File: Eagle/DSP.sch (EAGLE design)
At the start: 4 parts

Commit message: added lots of parts and connected things
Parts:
- added C4, C5: 0.1uF, kiss_z:C0603
- added D1: KWL-R1025VB, kiss_z:KWL-R1025VB
- added J1, J2, J4, J5: (no value), SparkFun-Connectors:CONN_02
- added J3: (no value), SparkFun-Connectors:CONN_11
- added R1: 4611X-101-102LF, kiss_z:4611X-101-102LF
- added R2, R3: 100K, kiss_z:R0603
- added U$1: NHD-C12864A1Z-FSW-FBW-HTT, kiss_z:NHD-C12864A1Z-FSW-FBW-HTT
- C2: value 0.1uF -> 0.22uF
- C3: value (none) -> 0.1uF
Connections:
- new net 18: J3.6, TEENSY_3.2.18
- new net 19: J3.7, TEENSY_3.2.19
- new net 20: J3.8, TEENSY_3.2.20
- new net 21: J3.9, TEENSY_3.2.21
- new net 22: J3.10, TEENSY_3.2.22
- new net ADC_IN: C2.2, J3.11, R2.2, R3.1, TEENSY_3.2.23
- new net CS_LCD: TEENSY_3.2.10, U$1./CS
- new net CS_PLL: J3.5, TEENSY_3.2.17
- new net CS_POT: J3.4, TEENSY_3.2.16
- new net DAC_OUT: C3.2, J2.1
- new net MISO: TEENSY_3.2.12
- new net MOSI: TEENSY_3.2.11, U$1.MOSI
- new net N$10: D1.P$8, R1.9
- new net N$11: D1.P$9, R1.10
- new net N$12: D1.P$10, R1.11
- new net N$13: D1.P$20, TEENSY_3.2.0
- new net N$14: D1.P$19, TEENSY_3.2.1
- new net N$15: D1.P$18, TEENSY_3.2.2
- new net N$16: D1.P$17, TEENSY_3.2.3
- new net N$17: D1.P$16, TEENSY_3.2.4
- new net N$18: D1.P$15, TEENSY_3.2.5
- new net N$19: D1.P$14, TEENSY_3.2.6
- new net N$20: D1.P$13, TEENSY_3.2.7
- new net N$21: D1.P$12, TEENSY_3.2.8
- new net N$22: D1.P$11, TEENSY_3.2.9
- new net N$3: D1.P$1, R1.2
- new net N$4: D1.P$2, R1.3
- new net N$5: D1.P$3, R1.4
- new net N$6: D1.P$4, R1.5
- new net N$7: D1.P$5, R1.6
- new net N$8: D1.P$6, R1.7
- new net N$9: D1.P$7, R1.8
- new net RDR_IN: C2.1, J5.1
- new net REG_LCD: TEENSY_3.2.15, U$1.A0
- new net RST_LCD: TEENSY_3.2.14, U$1./RESET
- new net SCLK: J3.3, TEENSY_3.2.13, U$1.SCLK
- net +3V3: now also C1.1, C5.1, J3.1, J4.1, R1.1, R2.1, U$1.LED+, U$1.VDD; no longer C2.1
- net +5V: now also C4.1, J1.1; no longer C1.1
- net GND: now also C4.2, C5.2, J1.2, J2.2, J3.2, J4.2, J5.2, R3.2, U$1.H-, U$1.LED-, U$1.VSS; no longer C2.2
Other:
- moved on the sheet: C1, C2, C3

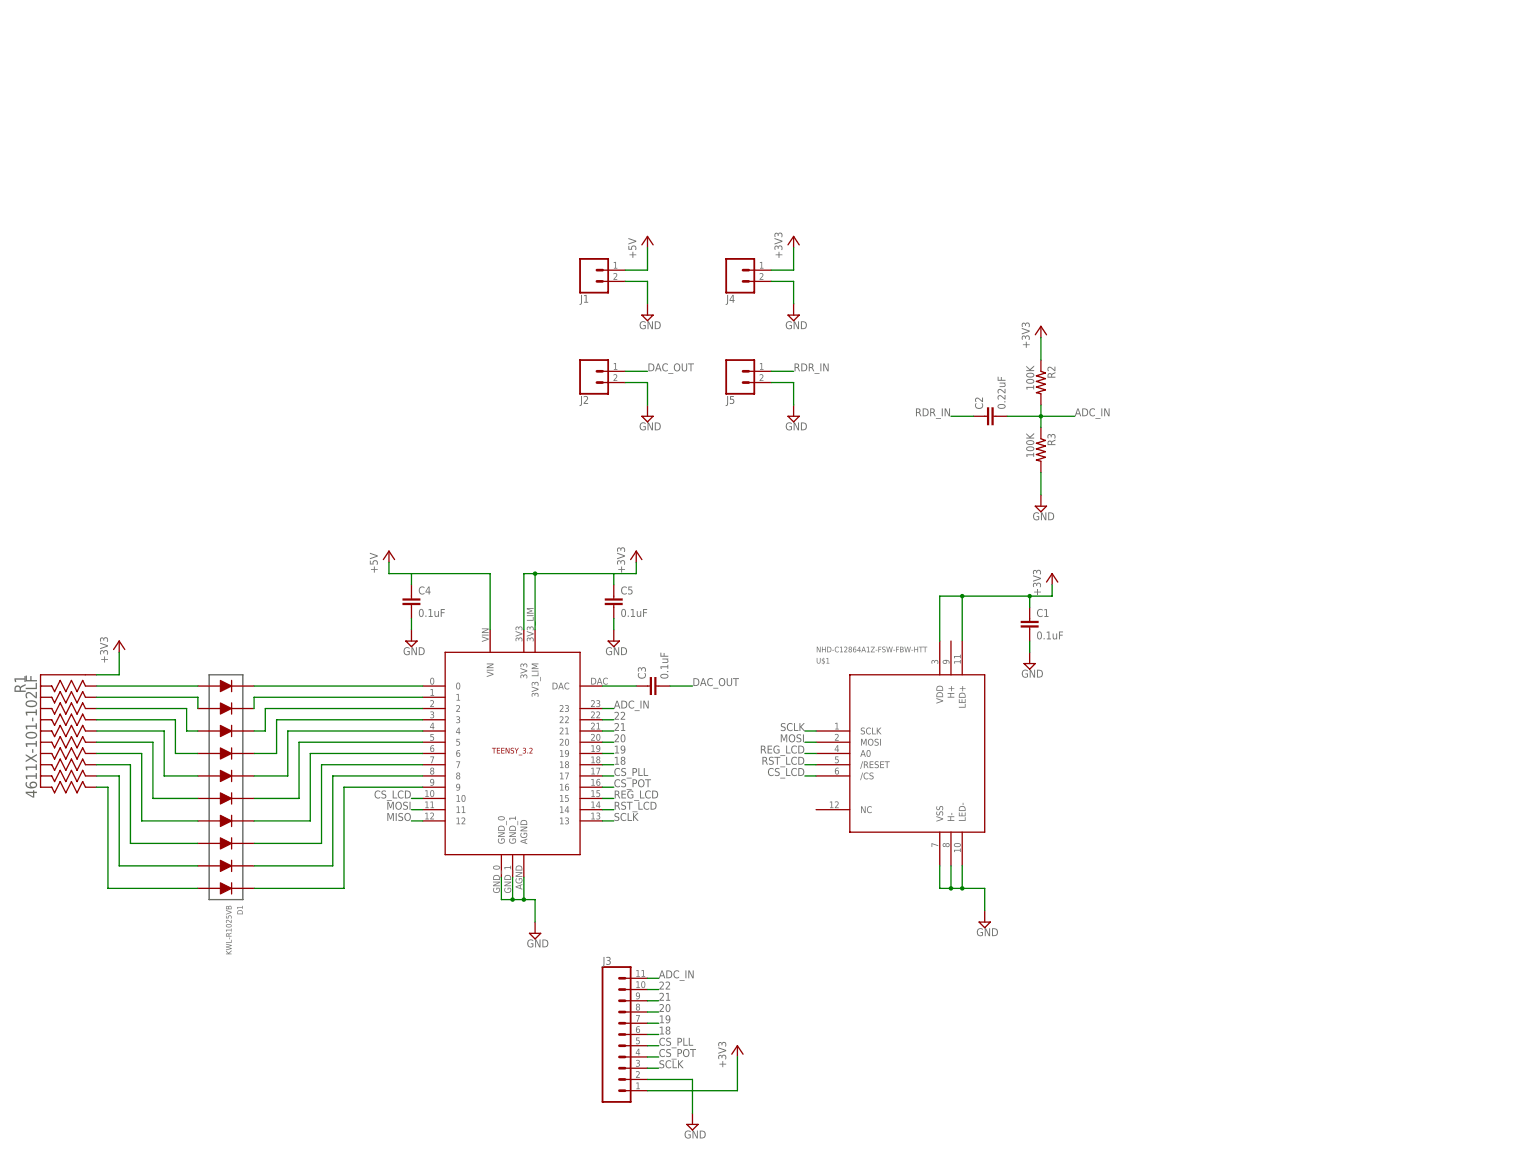
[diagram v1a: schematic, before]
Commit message: added switches
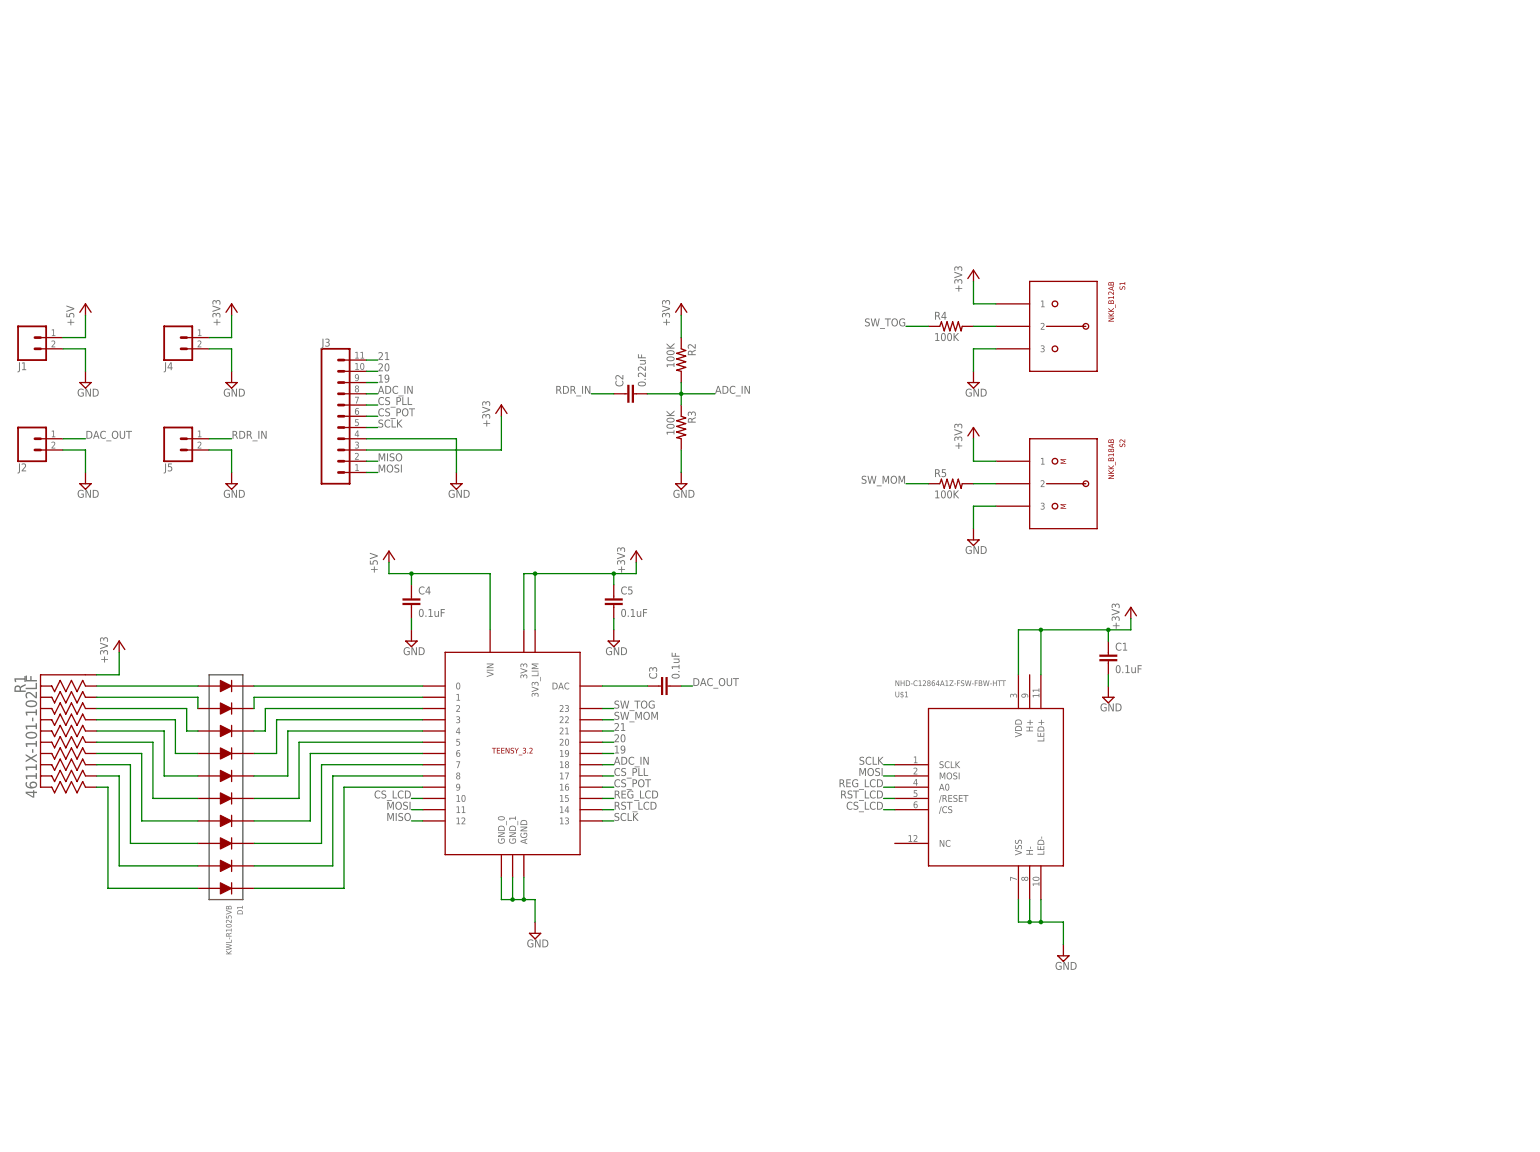
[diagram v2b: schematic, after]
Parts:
- added R4, R5: 100K, kiss_z:R0603
- added S1: NKK_B12AB, kiss_z:NKK_B12AB
- added S2: NKK_B18AB, kiss_z:NKK_B18AB
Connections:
- removed net 18: J3.6, TEENSY_3.2.18
- removed net 22: J3.10, TEENSY_3.2.22
- new net N$2: R5.2, S2.2
- new net N$23: R4.2, S1.2
- new net SW_MOM: R5.1, TEENSY_3.2.22
- new net SW_TOG: R4.1, TEENSY_3.2.23
- net +3V3: now also J3.3, S1.1, S2.1; no longer J3.1
- net 19: now also J3.9; no longer J3.7
- net 20: now also J3.10; no longer J3.8
- net 21: now also J3.11; no longer J3.9
- net ADC_IN: now also J3.8, TEENSY_3.2.18; no longer J3.11, TEENSY_3.2.23
- net CS_PLL: now also J3.7; no longer J3.5
- net CS_POT: now also J3.6; no longer J3.4
- net GND: now also J3.4, S1.3, S2.3; no longer J3.2
- net MISO: now also J3.2
- net MOSI: now also J3.1
- net SCLK: now also J3.5; no longer J3.3
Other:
- moved on the sheet: C1, C2, C3, J1, J2, J3, J4, J5, R2, R3, U$1

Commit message: continuing layout
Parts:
- added C6: 0.1uF, kiss_z:C0603
- added R6, R7: 100K, kiss_z:R0603
- R1: value 4611X-101-102LF -> 4711X_RES; device kiss_z:4611X-101-102LF -> kiss_z:4711X_RES
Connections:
- net +3V3: now also C6.1, R6.2
- net GND: now also R7.1
- net N$2: now also R6.1, R7.2
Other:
- moved on the sheet: R4, R5, S1, S2
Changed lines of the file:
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@@
 <part name="+3V1" library="supply1" library_urn="urn:adsk.eagle:library:371" deviceset="+3V3" device=""/>
 <part name="C3" library="kiss_z" deviceset="C0603" device="" value="0.1uF"/>
-<part name="R1" library="kiss_z" deviceset="4611X-101-102LF" device=""/>
+<part name="R1" library="kiss_z" deviceset="4711X_RES" device=""/>
 <part name="D1" library="kiss_z" deviceset="KWL-R1025VB" device=""/>
 <part name="+3V3" library="supply1" library_urn="urn:adsk.eagle:library:371" deviceset="+3V3" device=""/>
@@
 <part name="+3V8" library="supply1" library_urn="urn:adsk.eagle:library:371" deviceset="+3V3" device=""/>
 <part name="SUPPLY13" library="supply2" library_urn="urn:adsk.eagle:library:372" deviceset="GND" device=""/>
+<part name="R6" library="kiss_z" deviceset="R0603" device="" value="100K"/>
+<part name="R7" library="kiss_z" deviceset="R0603" device="" value="100K"/>
+<part name="C6" library="kiss_z" deviceset="C0603" device="" value="0.1uF"/>
+<part name="SUPPLY14" library="supply2" library_urn="urn:adsk.eagle:library:372" deviceset="GND" device=""/>
 </parts>
 <sheets>
@@
 <instance part="SUPPLY4" gate="GND" x="40.64" y="71.12"/>
 <instance part="SUPPLY5" gate="GND" x="86.36" y="71.12"/>
-<instance part="+3V2" gate="G$1" x="203.2" y="78.74"/>
+<instance part="+3V2" gate="G$1" x="213.36" y="78.74"/>
 <instance part="C1" gate="G$1" x="198.12" y="68.58"/>
 <instance part="SUPPLY2" gate="GND" x="198.12" y="58.42"/>
@@
 <instance part="P+2" gate="1" x="-33.02" y="147.32"/>
 <instance part="J3" gate="G$1" x="20.32" y="121.92"/>
-<instance part="S1" gate="A" x="180.34" y="152.4" rot="R270"/>
-<instance part="S2" gate="A" x="180.34" y="116.84" rot="R270"/>
-<instance part="R4" gate="G$1" x="162.56" y="142.24"/>
-<instance part="R5" gate="G$1" x="162.56" y="106.68"/>
-<instance part="+3V7" gate="G$1" x="167.64" y="154.94"/>
-<instance part="SUPPLY12" gate="GND" x="167.64" y="129.54"/>
-<instance part="+3V8" gate="G$1" x="167.64" y="119.38"/>
-<instance part="SUPPLY13" gate="GND" x="167.64" y="93.98"/>
+<instance part="S1" gate="A" x="175.26" y="154.94" rot="R270"/>
+<instance part="S2" gate="A" x="175.26" y="111.76" rot="R270"/>
+<instance part="R4" gate="G$1" x="157.48" y="144.78"/>
+<instance part="R5" gate="G$1" x="142.24" y="101.6"/>
+<instance part="+3V7" gate="G$1" x="162.56" y="157.48"/>
+<instance part="SUPPLY12" gate="GND" x="162.56" y="132.08"/>
+<instance part="+3V8" gate="G$1" x="162.56" y="121.92"/>
+<instance part="SUPPLY13" gate="GND" x="162.56" y="81.28"/>
+<instance part="R6" gate="G$1" x="149.86" y="109.22" rot="R90"/>
+<instance part="R7" gate="G$1" x="149.86" y="93.98" rot="R90"/>
+<instance part="C6" gate="G$1" x="208.28" y="68.58"/>
+<instance part="SUPPLY14" gate="GND" x="208.28" y="58.42"/>
 </instances>
 <busses>
@@
 <segment>
 <pinref part="SUPPLY13" gate="GND" pin="GND"/>
-<wire x1="167.64" y1="96.52" x2="167.64" y2="101.6" width="0.1524" layer="91"/>
+<wire x1="162.56" y1="83.82" x2="162.56" y2="86.36" width="0.1524" layer="91"/>
 <pinref part="S2" gate="A" pin="3"/>
-<wire x1="167.64" y1="101.6" x2="172.72" y2="101.6" width="0.1524" layer="91"/>
+<wire x1="162.56" y1="86.36" x2="162.56" y2="96.52" width="0.1524" layer="91"/>
+<wire x1="162.56" y1="96.52" x2="167.64" y2="96.52" width="0.1524" layer="91"/>
+<pinref part="R7" gate="G$1" pin="1"/>
+<wire x1="149.86" y1="88.9" x2="149.86" y2="86.36" width="0.1524" layer="91"/>
+<wire x1="149.86" y1="86.36" x2="162.56" y2="86.36" width="0.1524" layer="91"/>
+<junction x="162.56" y="86.36"/>
 </segment>
 <segment>
 <pinref part="SUPPLY12" gate="GND" pin="GND"/>
-<wire x1="167.64" y1="132.08" x2="167.64" y2="137.16" width="0.1524" layer="91"/>
+<wire x1="162.56" y1="134.62" x2="162.56" y2="139.7" width="0.1524" layer="91"/>
 <pinref part="S1" gate="A" pin="3"/>
-<wire x1="167.64" y1="137.16" x2="172.72" y2="137.16" width="0.1524" layer="91"/>
+<wire x1="162.56" y1="139.7" x2="167.64" y2="139.7" width="0.1524" layer="91"/>
+</segment>
+<segment>
+<pinref part="SUPPLY14" gate="GND" pin="GND"/>
+<wire x1="208.28" y1="60.96" x2="208.28" y2="63.5" width="0.1524" layer="91"/>
 </segment>
 </net>
@@
 </segment>
 <segment>
+<pinref part="+3V4" gate="G$1" pin="+3V3"/>
+<pinref part="R2" gate="G$1" pin="1"/>
+<wire x1="101.6" y1="144.78" x2="101.6" y2="139.7" width="0.1524" layer="91"/>
+</segment>
+<segment>
+<pinref part="+3V5" gate="G$1" pin="+3V3"/>
+<wire x1="60.96" y1="121.92" x2="60.96" y2="114.3" width="0.1524" layer="91"/>
+<wire x1="60.96" y1="114.3" x2="30.48" y2="114.3" width="0.1524" layer="91"/>
+<pinref part="J3" gate="G$1" pin="3"/>
+</segment>
+<segment>
+<pinref part="J4" gate="G$1" pin="1"/>
+<pinref part="+3V6" gate="G$1" pin="+3V3"/>
+<wire x1="-5.08" y1="139.7" x2="0" y2="139.7" width="0.1524" layer="91"/>
+<wire x1="0" y1="139.7" x2="0" y2="144.78" width="0.1524" layer="91"/>
+</segment>
+<segment>
+<pinref part="+3V8" gate="G$1" pin="+3V3"/>
+<wire x1="162.56" y1="119.38" x2="162.56" y2="116.84" width="0.1524" layer="91"/>
+<pinref part="S2" gate="A" pin="1"/>
+<wire x1="162.56" y1="116.84" x2="162.56" y2="106.68" width="0.1524" layer="91"/>
+<wire x1="162.56" y1="106.68" x2="167.64" y2="106.68" width="0.1524" layer="91"/>
+<wire x1="162.56" y1="116.84" x2="149.86" y2="116.84" width="0.1524" layer="91"/>
+<junction x="162.56" y="116.84"/>
+<pinref part="R6" gate="G$1" pin="2"/>
+<wire x1="149.86" y1="116.84" x2="149.86" y2="114.3" width="0.1524" layer="91"/>
+</segment>
+<segment>
+<pinref part="+3V7" gate="G$1" pin="+3V3"/>
+<wire x1="162.56" y1="154.94" x2="162.56" y2="149.86" width="0.1524" layer="91"/>
+<pinref part="S1" gate="A" pin="1"/>
+<wire x1="162.56" y1="149.86" x2="167.64" y2="149.86" width="0.1524" layer="91"/>
+</segment>
+<segment>
 <pinref part="+3V2" gate="G$1" pin="+3V3"/>
-<wire x1="203.2" y1="76.2" x2="203.2" y2="73.66" width="0.1524" layer="91"/>
-<wire x1="203.2" y1="73.66" x2="198.12" y2="73.66" width="0.1524" layer="91"/>
+<wire x1="213.36" y1="76.2" x2="213.36" y2="73.66" width="0.1524" layer="91"/>
+<wire x1="213.36" y1="73.66" x2="208.28" y2="73.66" width="0.1524" layer="91"/>
 <pinref part="C1" gate="G$1" pin="1"/>
+<wire x1="208.28" y1="73.66" x2="198.12" y2="73.66" width="0.1524" layer="91"/>
 <wire x1="198.12" y1="73.66" x2="198.12" y2="71.12" width="0.1524" layer="91"/>
 <wire x1="198.12" y1="73.66" x2="182.88" y2="73.66" width="0.1524" layer="91"/>
@@
 <pinref part="U$1" gate="A" pin="VDD"/>
 <wire x1="177.8" y1="73.66" x2="177.8" y2="63.5" width="0.1524" layer="91"/>
-</segment>
-<segment>
-<pinref part="+3V4" gate="G$1" pin="+3V3"/>
-<pinref part="R2" gate="G$1" pin="1"/>
-<wire x1="101.6" y1="144.78" x2="101.6" y2="139.7" width="0.1524" layer="91"/>
-</segment>
-<segment>
-<pinref part="+3V5" gate="G$1" pin="+3V3"/>
-<wire x1="60.96" y1="121.92" x2="60.96" y2="114.3" width="0.1524" layer="91"/>
-<wire x1="60.96" y1="114.3" x2="30.48" y2="114.3" width="0.1524" layer="91"/>
-<pinref part="J3" gate="G$1" pin="3"/>
-</segment>
-<segment>
-<pinref part="J4" gate="G$1" pin="1"/>
-<pinref part="+3V6" gate="G$1" pin="+3V3"/>
-<wire x1="-5.08" y1="139.7" x2="0" y2="139.7" width="0.1524" layer="91"/>
-<wire x1="0" y1="139.7" x2="0" y2="144.78" width="0.1524" layer="91"/>
-</segment>
-<segment>
-<pinref part="+3V8" gate="G$1" pin="+3V3"/>
-<wire x1="167.64" y1="116.84" x2="167.64" y2="111.76" width="0.1524" layer="91"/>
-<pinref part="S2" gate="A" pin="1"/>
-<wire x1="167.64" y1="111.76" x2="172.72" y2="111.76" width="0.1524" layer="91"/>
-</segment>
-<segment>
-<pinref part="+3V7" gate="G$1" pin="+3V3"/>
-<wire x1="167.64" y1="152.4" x2="167.64" y2="147.32" width="0.1524" layer="91"/>
-<pinref part="S1" gate="A" pin="1"/>
-<wire x1="167.64" y1="147.32" x2="172.72" y2="147.32" width="0.1524" layer="91"/>
+<pinref part="C6" gate="G$1" pin="1"/>
+<wire x1="208.28" y1="73.66" x2="208.28" y2="71.12" width="0.1524" layer="91"/>
+<junction x="208.28" y="73.66"/>
 </segment>
 </net>
@@
 <segment>
 <pinref part="R4" gate="G$1" pin="1"/>
-<wire x1="152.4" y1="142.24" x2="157.48" y2="142.24" width="0.1524" layer="91"/>
-<label x="152.4" y="142.24" size="1.778" layer="95" rot="MR0"/>
+<wire x1="147.32" y1="144.78" x2="152.4" y2="144.78" width="0.1524" layer="91"/>
+<label x="147.32" y="144.78" size="1.778" layer="95" rot="MR0"/>
 </segment>
 </net>
@@
 <segment>
 <pinref part="R5" gate="G$1" pin="1"/>
-<wire x1="152.4" y1="106.68" x2="157.48" y2="106.68" width="0.1524" layer="91"/>
-<label x="152.4" y="106.68" size="1.778" layer="95" rot="MR0"/>
+<wire x1="132.08" y1="101.6" x2="137.16" y2="101.6" width="0.1524" layer="91"/>
+<label x="132.08" y="101.6" size="1.778" layer="95" rot="MR0"/>
 </segment>
 </net>
@@
 <pinref part="S2" gate="A" pin="2"/>
 <pinref part="R5" gate="G$1" pin="2"/>
-<wire x1="167.64" y1="106.68" x2="172.72" y2="106.68" width="0.1524" layer="91"/>
+<wire x1="147.32" y1="101.6" x2="149.86" y2="101.6" width="0.1524" layer="91"/>
+<pinref part="R7" gate="G$1" pin="2"/>
+<wire x1="149.86" y1="101.6" x2="167.64" y2="101.6" width="0.1524" layer="91"/>
+<wire x1="149.86" y1="99.06" x2="149.86" y2="101.6" width="0.1524" layer="91"/>
+<junction x="149.86" y="101.6"/>
+<pinref part="R6" gate="G$1" pin="1"/>
+<wire x1="149.86" y1="101.6" x2="149.86" y2="104.14" width="0.1524" layer="91"/>
 </segment>
 </net>
@@
 <pinref part="S1" gate="A" pin="2"/>
 <pinref part="R4" gate="G$1" pin="2"/>
-<wire x1="167.64" y1="142.24" x2="172.72" y2="142.24" width="0.1524" layer="91"/>
-</segment>
-</net>
+<wire x1="162.56" y1="144.78" x2="167.64" y2="144.78" width="0.1524" layer="91"/>
+</segment>
+</net>
